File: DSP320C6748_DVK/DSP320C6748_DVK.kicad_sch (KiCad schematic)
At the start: 0 parts

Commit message: Power section schematic Partially completed
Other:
- sheet DSP renamed DSP_POWER
- added sheet DSP-I (DSP-I.kicad_sch)
- added sheet DSP-II (DSP-II.kicad_sch)
- added sheet Power_Supply (Power_Supply.kicad_sch)
- sheet DSP_POWER: file DSP.kicad_sch -> DSP_POWER.kicad_sch
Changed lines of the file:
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@@
+	)
+	(sheet
+		(at 177.8 24.13)
+		(size 65.532 67.818)
+		(exclude_from_sim no)
+		(in_bom yes)
+		(on_board yes)
+		(dnp no)
+		(fields_autoplaced yes)
+		(stroke
+			(width 0.1524)
+			(type solid)
+		)
+		(fill
+			(color 0 0 0 0.0000)
+		)
+		(property "Sheetname" "DSP-II"
+			(at 177.8 23.4184 0)
+			(effects
+				(font
+					(size 1.27 1.27)
+				)
+				(justify left bottom)
+			)
+		)
+		(property "Sheetfile" "DSP-II.kicad_sch"
+			(at 177.8 92.5326 0)
+			(effects
+				(font
+					(size 1.27 1.27)
+				)
+				(justify left top)
+			)
+		)
+		(instances
+			(project "DSP320C6748_DVK"
+				(path "/3a70ffc0-9fe7-4a5b-b3c2-23140355df82"
+					(page "4")
+				)
+			)
+		)
+	)
+	(sheet
+		(at 100.33 24.13)
+		(size 65.532 67.818)
+		(exclude_from_sim no)
+		(in_bom yes)
+		(on_board yes)
+		(dnp no)
+		(fields_autoplaced yes)
+		(stroke
+			(width 0.1524)
+			(type solid)
+		)
+		(fill
+			(color 0 0 0 0.0000)
+		)
+		(property "Sheetname" "DSP-I"
+			(at 100.33 23.4184 0)
+			(effects
+				(font
+					(size 1.27 1.27)
+				)
+				(justify left bottom)
+			)
+		)
+		(property "Sheetfile" "DSP-I.kicad_sch"
+			(at 100.33 92.5326 0)
+			(effects
+				(font
+					(size 1.27 1.27)
+				)
+				(justify left top)
+			)
+		)
+		(instances
+			(project "DSP320C6748_DVK"
+				(path "/3a70ffc0-9fe7-4a5b-b3c2-23140355df82"
+					(page "3")
+				)
+			)
+		)
 	)
 	(sheet
@@
 			(color 0 0 0 0.0000)
 		)
-		(property "Sheetname" "DSP"
+		(property "Sheetname" "DSP_POWER"
 			(at 26.162 22.9104 0)
 			(effects
@@
 			)
 		)
-		(property "Sheetfile" "DSP.kicad_sch"
+		(property "Sheetfile" "DSP_POWER.kicad_sch"
 			(at 26.162 92.0246 0)
 			(effects
@@
 				)
 			)
+		)
+	)
+	(sheet
+		(at 26.67 102.87)
+		(size 20.32 19.05)
+		(exclude_from_sim no)
+		(in_bom yes)
+		(on_board yes)
+		(dnp no)
+		(fields_autoplaced yes)
+		(stroke
+			(width 0.1524)
+			(type solid)
+		)
+		(fill
+			(color 0 0 0 0.0000)
+		)
+		(property "Sheetname" "Power_Supply"
+			(at 26.67 102.1584 0)
+			(effects
+				(font
+					(size 1.27 1.27)
+				)
+				(justify left bottom)
+			)
+		)
+		(property "Sheetfile" "Power_Supply.kicad_sch"
+			(at 26.67 122.5046 0)
+			(effects
+				(font
+					(size 1.27 1.27)
+				)
+				(justify left top)
+			)
+		)
+		(instances
+			(project "DSP320C6748_DVK"
+				(path "/3a70ffc0-9fe7-4a5b-b3c2-23140355df82"
+					(page "5")
+				)
+			)

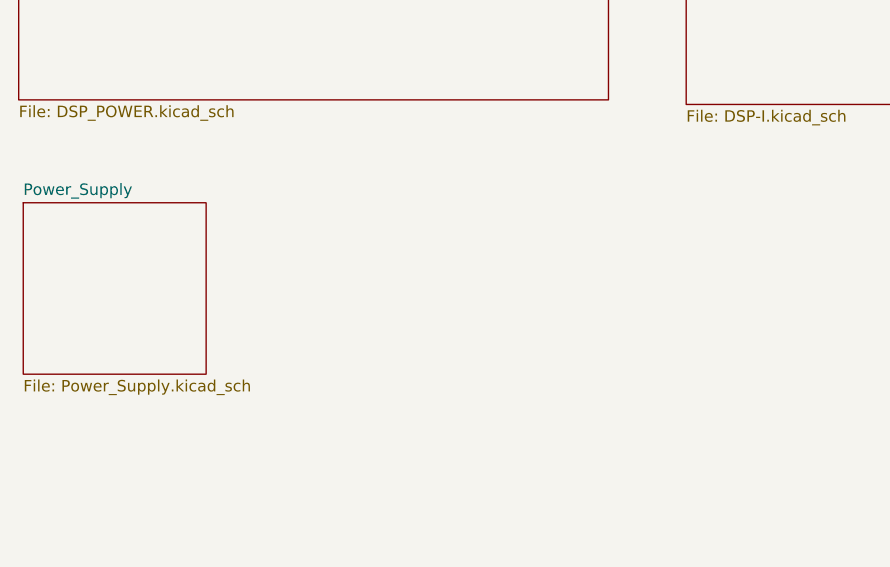
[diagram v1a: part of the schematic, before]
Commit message: TPS650250 Section Added
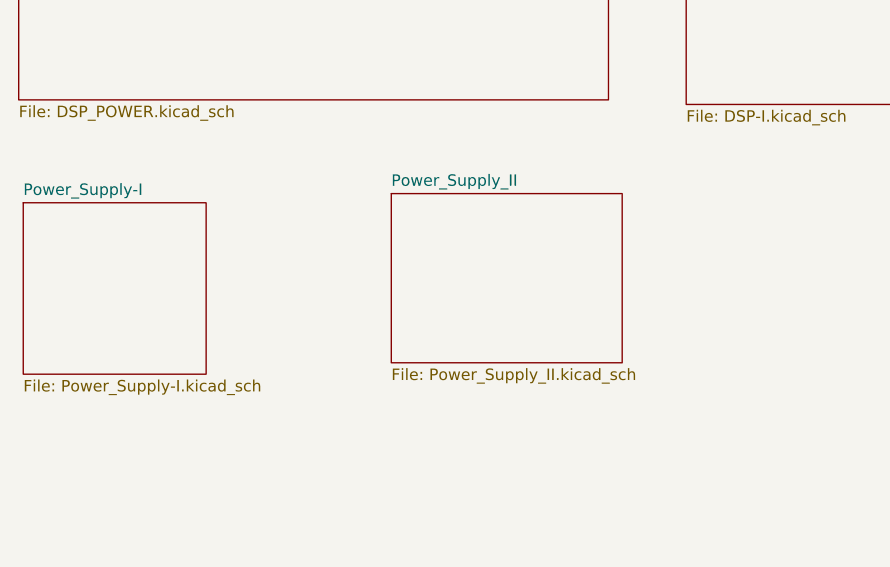
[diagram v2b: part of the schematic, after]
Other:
- sheet Power_Supply renamed Power_Supply-I
- added sheet Power_Supply_II (Power_Supply_II.kicad_sch)
- sheet Power_Supply-I: file Power_Supply.kicad_sch -> Power_Supply-I.kicad_sch
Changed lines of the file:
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@@
 			(color 0 0 0 0.0000)
 		)
-		(property "Sheetname" "Power_Supply"
+		(property "Sheetname" "Power_Supply-I"
 			(at 26.67 102.1584 0)
 			(effects
@@
 			)
 		)
-		(property "Sheetfile" "Power_Supply.kicad_sch"
+		(property "Sheetfile" "Power_Supply-I.kicad_sch"
 			(at 26.67 122.5046 0)
 			(effects
@@
 				)
 			)
+		)
+	)
+	(sheet
+		(at 67.564 101.854)
+		(size 25.654 18.796)
+		(exclude_from_sim no)
+		(in_bom yes)
+		(on_board yes)
+		(dnp no)
+		(fields_autoplaced yes)
+		(stroke
+			(width 0.1524)
+			(type solid)
+		)
+		(fill
+			(color 0 0 0 0.0000)
+		)
+		(property "Sheetname" "Power_Supply_II"
+			(at 67.564 101.1424 0)
+			(effects
+				(font
+					(size 1.27 1.27)
+				)
+				(justify left bottom)
+			)
+		)
+		(property "Sheetfile" "Power_Supply_II.kicad_sch"
+			(at 67.564 121.2346 0)
+			(effects
+				(font
+					(size 1.27 1.27)
+				)
+				(justify left top)
+			)
+		)
+		(instances
+			(project "DSP320C6748_DVK"
+				(path "/3a70ffc0-9fe7-4a5b-b3c2-23140355df82"
+					(page "6")
+				)
+			)

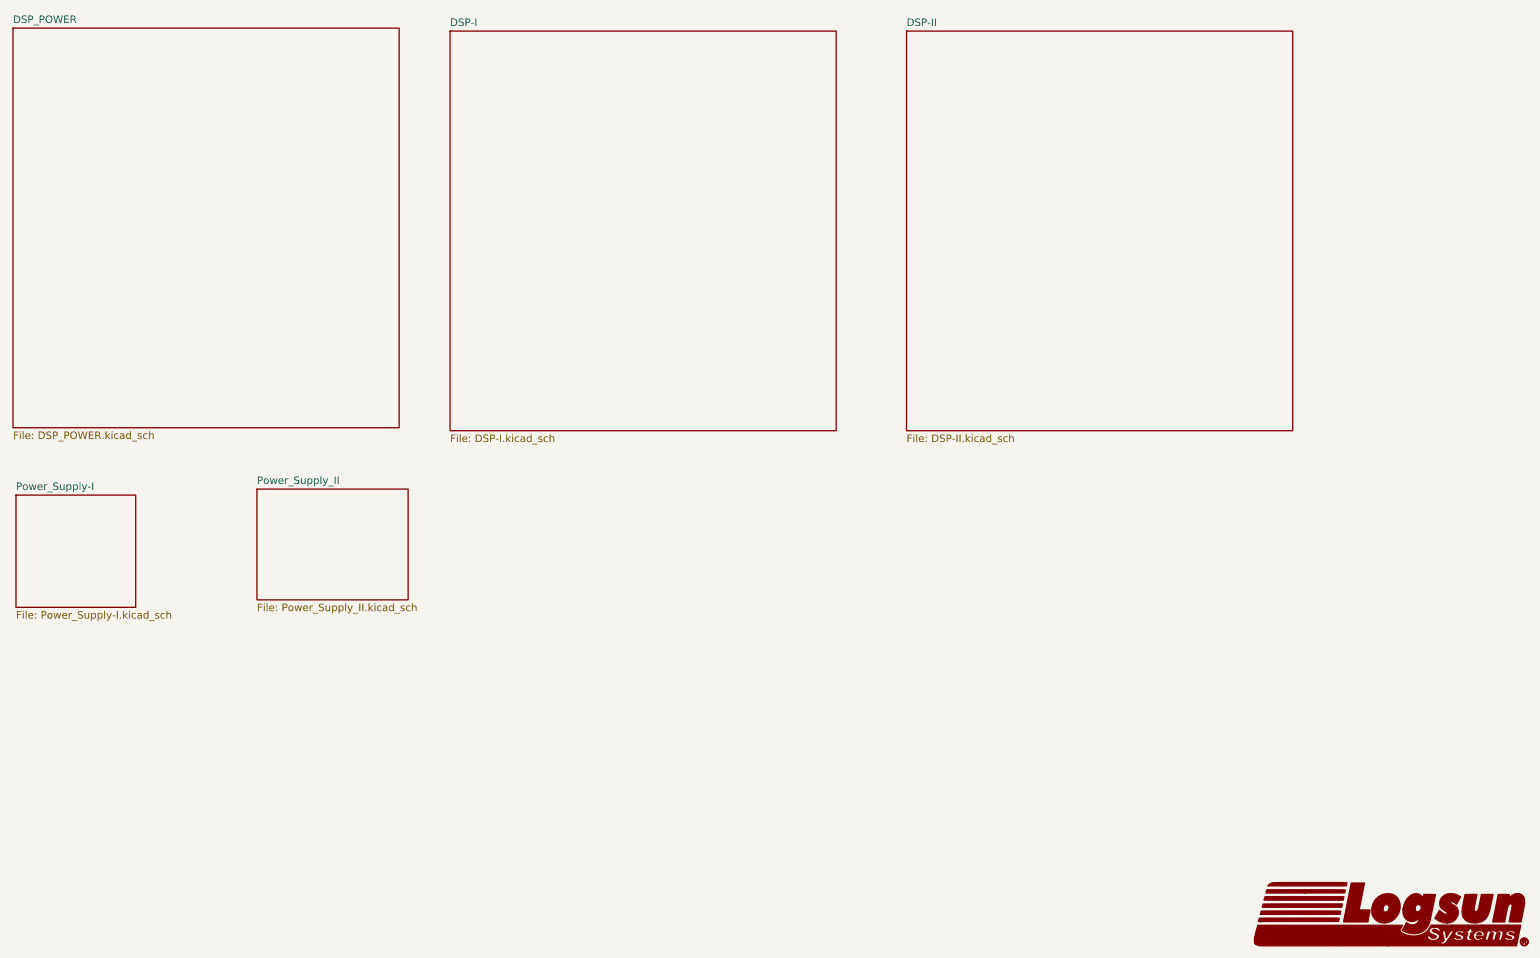
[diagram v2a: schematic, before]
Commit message: Partial Serial Circuit Added
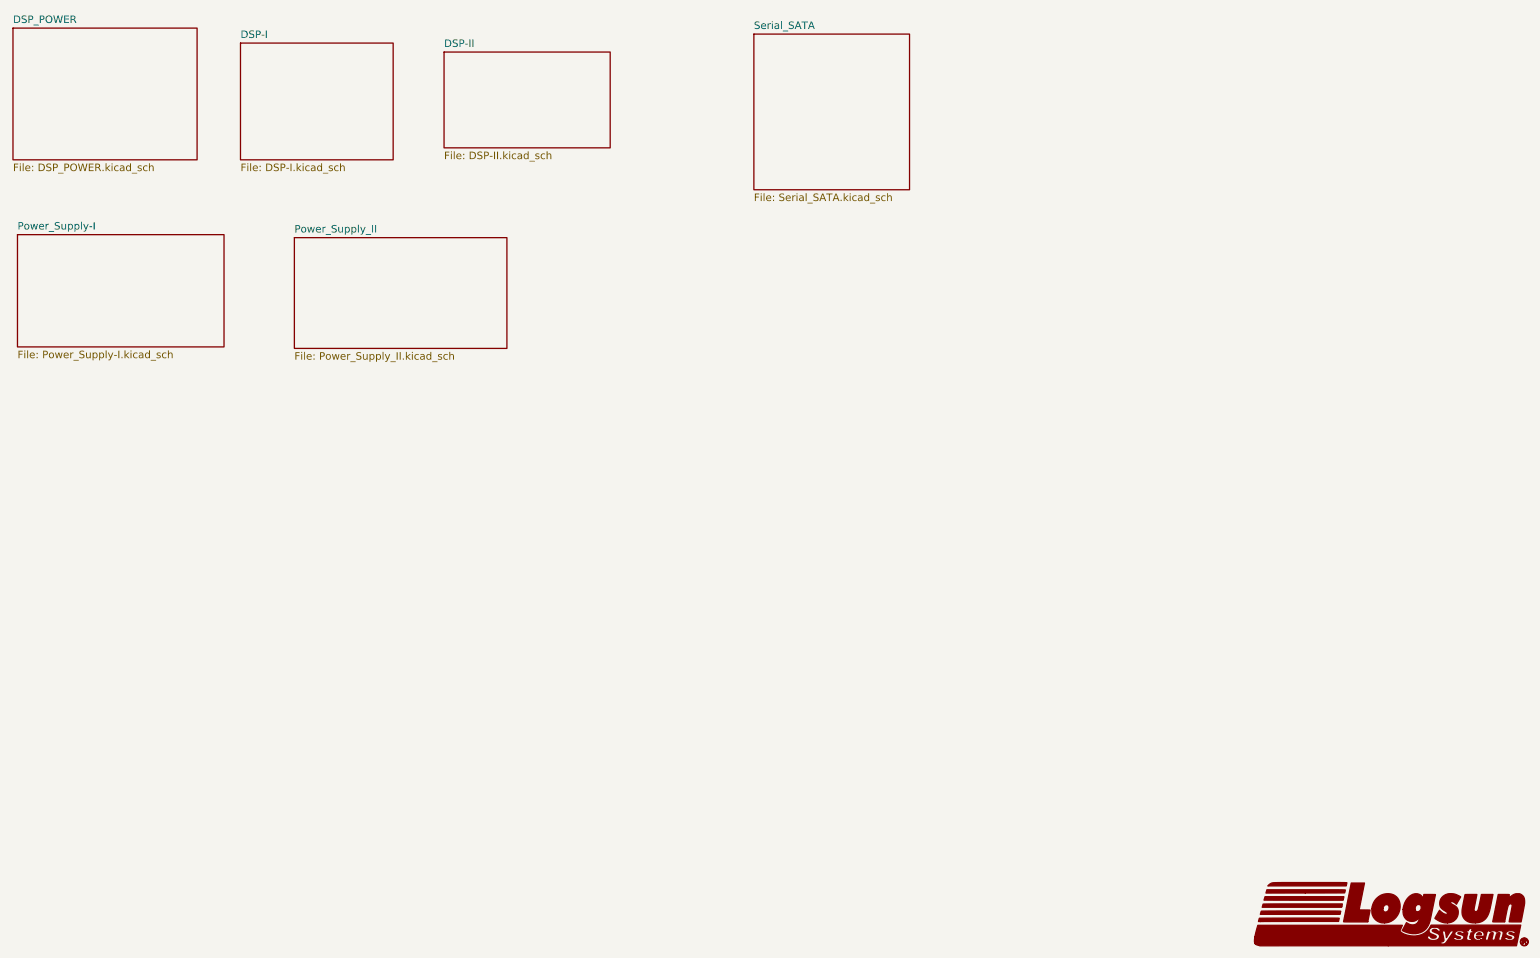
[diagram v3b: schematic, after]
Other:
- added sheet Serial_SATA (Serial_SATA.kicad_sch)
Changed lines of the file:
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@@
 	)
 	(sheet
-		(at 177.8 24.13)
-		(size 65.532 67.818)
+		(at 151.892 24.638)
+		(size 26.416 26.416)
+		(exclude_from_sim no)
+		(in_bom yes)
+		(on_board yes)
+		(dnp no)
+		(fields_autoplaced yes)
+		(stroke
+			(width 0.1524)
+			(type solid)
+		)
+		(fill
+			(color 0 0 0 0.0000)
+		)
+		(property "Sheetname" "Serial_SATA"
+			(at 151.892 23.9264 0)
+			(effects
+				(font
+					(size 1.27 1.27)
+				)
+				(justify left bottom)
+			)
+		)
+		(property "Sheetfile" "Serial_SATA.kicad_sch"
+			(at 151.892 51.6386 0)
+			(effects
+				(font
+					(size 1.27 1.27)
+				)
+				(justify left top)
+			)
+		)
+		(instances
+			(project "DSP320C6748_DVK"
+				(path "/3a70ffc0-9fe7-4a5b-b3c2-23140355df82"
+					(page "7")
+				)
+			)
+		)
+	)
+	(sheet
+		(at 99.314 27.686)
+		(size 28.194 16.256)
 		(exclude_from_sim no)
 		(in_bom yes)
@@
 		)
 		(property "Sheetname" "DSP-II"
-			(at 177.8 23.4184 0)
+			(at 99.314 26.9744 0)
 			(effects
 				(font
@@
 		)
 		(property "Sheetfile" "DSP-II.kicad_sch"
-			(at 177.8 92.5326 0)
+			(at 99.314 44.5266 0)
 			(effects
 				(font
@@
 	)
 	(sheet
-		(at 100.33 24.13)
-		(size 65.532 67.818)
+		(at 64.77 26.162)
+		(size 25.908 19.812)
 		(exclude_from_sim no)
 		(in_bom yes)
@@
 		)
 		(property "Sheetname" "DSP-I"
-			(at 100.33 23.4184 0)
+			(at 64.77 25.4504 0)
 			(effects
 				(font
@@
 		)
 		(property "Sheetfile" "DSP-I.kicad_sch"
-			(at 100.33 92.5326 0)
+			(at 64.77 46.5586 0)
 			(effects
 				(font
@@
 	(sheet
 		(at 26.162 23.622)
-		(size 65.532 67.818)
+		(size 31.242 22.352)
 		(exclude_from_sim no)
 		(in_bom yes)
@@
 		)
 		(property "Sheetfile" "DSP_POWER.kicad_sch"
-			(at 26.162 92.0246 0)
+			(at 26.162 46.5586 0)
 			(effects
 				(font
@@
 	)
 	(sheet
-		(at 26.67 102.87)
-		(size 20.32 19.05)
+		(at 26.924 58.674)
+		(size 35.052 19.05)
 		(exclude_from_sim no)
 		(in_bom yes)
@@
 		)
 		(property "Sheetname" "Power_Supply-I"
-			(at 26.67 102.1584 0)
+			(at 26.924 57.9624 0)
 			(effects
 				(font
@@
 		)
 		(property "Sheetfile" "Power_Supply-I.kicad_sch"
-			(at 26.67 122.5046 0)
+			(at 26.924 78.3086 0)
 			(effects
 				(font
@@
 	)
 	(sheet
-		(at 67.564 101.854)
-		(size 25.654 18.796)
+		(at 73.914 59.182)
+		(size 36.068 18.796)
 		(exclude_from_sim no)
 		(in_bom yes)
@@
 		)
 		(property "Sheetname" "Power_Supply_II"
-			(at 67.564 101.1424 0)
+			(at 73.914 58.4704 0)
 			(effects
 				(font
@@
 		)
 		(property "Sheetfile" "Power_Supply_II.kicad_sch"
-			(at 67.564 121.2346 0)
-			(effects
-				(font
+			(at 73.914 78.5626 0)
+			(effects
+				(font

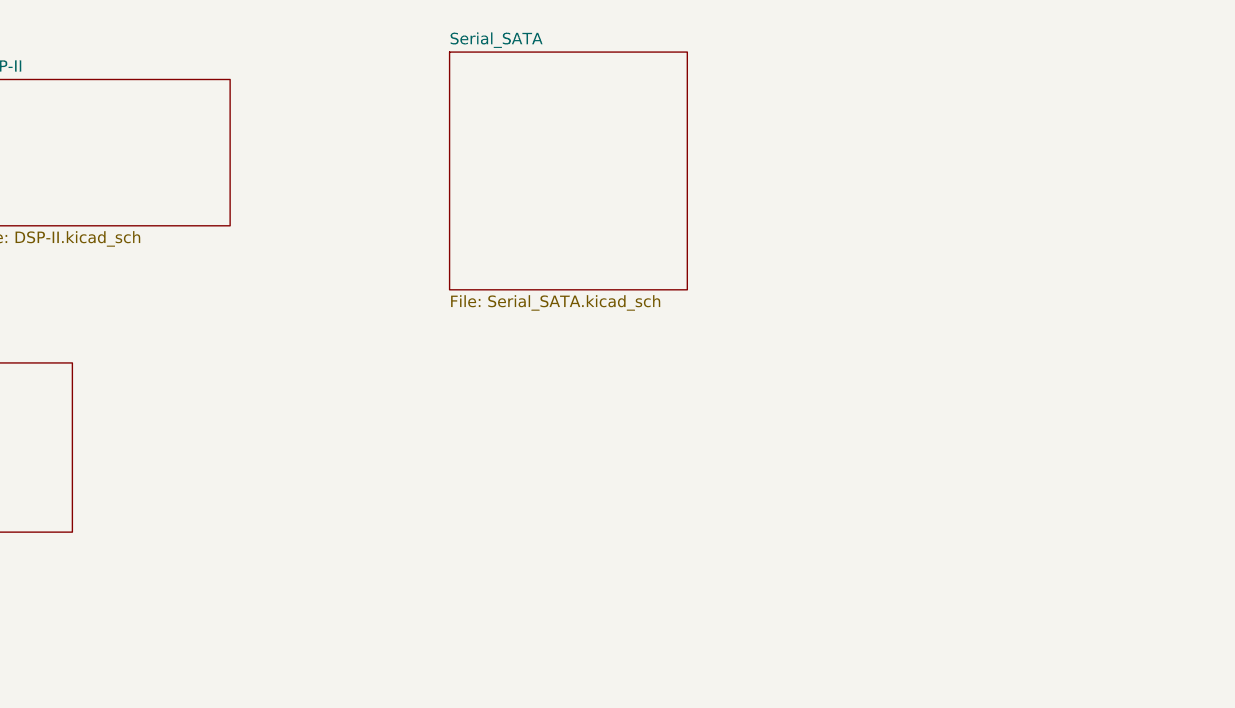
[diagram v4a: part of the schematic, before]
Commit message: Partial VGA-LCD schematic added
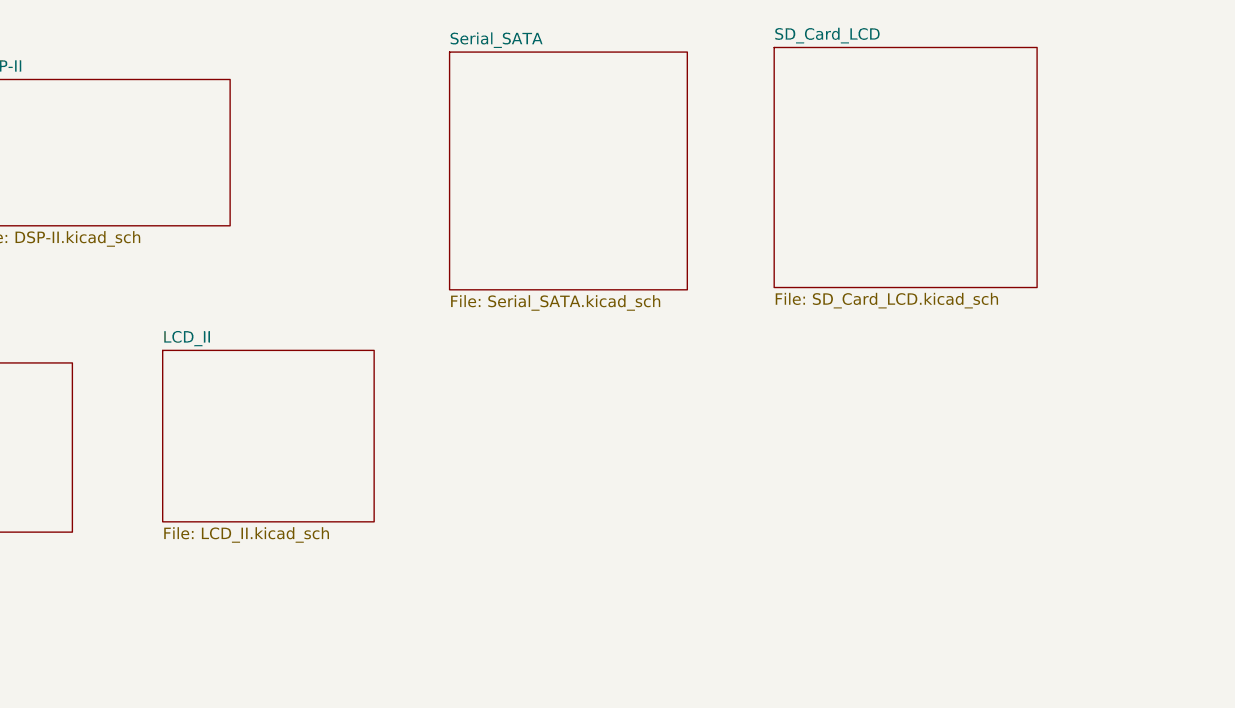
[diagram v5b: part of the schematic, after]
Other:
- added sheet LCD_II (LCD_II.kicad_sch)
- added sheet SD_Card_LCD (SD_Card_LCD.kicad_sch)
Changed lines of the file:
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@@
+	)
+	(sheet
+		(at 120.015 57.785)
+		(size 23.495 19.05)
+		(exclude_from_sim no)
+		(in_bom yes)
+		(on_board yes)
+		(dnp no)
+		(fields_autoplaced yes)
+		(stroke
+			(width 0.1524)
+			(type solid)
+		)
+		(fill
+			(color 0 0 0 0)
+		)
+		(property "Sheetname" "LCD_II"
+			(at 120.015 57.0734 0)
+			(show_name no)
+			(do_not_autoplace no)
+			(effects
+				(font
+					(size 1.27 1.27)
+				)
+				(justify left bottom)
+			)
+		)
+		(property "Sheetfile" "LCD_II.kicad_sch"
+			(at 120.015 77.4196 0)
+			(show_name no)
+			(do_not_autoplace no)
+			(effects
+				(font
+					(size 1.27 1.27)
+				)
+				(justify left top)
+			)
+		)
+		(instances
+			(project "DSP320C6748_DVK"
+				(path "/3a70ffc0-9fe7-4a5b-b3c2-23140355df82"
+					(page "9")
+				)
+			)
+		)
+	)
+	(sheet
+		(at 187.96 24.13)
+		(size 29.21 26.67)
+		(exclude_from_sim no)
+		(in_bom yes)
+		(on_board yes)
+		(dnp no)
+		(fields_autoplaced yes)
+		(stroke
+			(width 0.1524)
+			(type solid)
+		)
+		(fill
+			(color 0 0 0 0)
+		)
+		(property "Sheetname" "SD_Card_LCD"
+			(at 187.96 23.4184 0)
+			(show_name no)
+			(do_not_autoplace no)
+			(effects
+				(font
+					(size 1.27 1.27)
+				)
+				(justify left bottom)
+			)
+		)
+		(property "Sheetfile" "SD_Card_LCD.kicad_sch"
+			(at 187.96 51.3846 0)
+			(show_name no)
+			(do_not_autoplace no)
+			(effects
+				(font
+					(size 1.27 1.27)
+				)
+				(justify left top)
+			)
+		)
+		(instances
+			(project "DSP320C6748_DVK"
+				(path "/3a70ffc0-9fe7-4a5b-b3c2-23140355df82"
+					(page "8")
+				)
+			)
+		)
 	)
 	(sheet
